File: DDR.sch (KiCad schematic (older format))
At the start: 41 parts, among them U1 IMX6UL_BGA289, U2 DDR3_BGA96

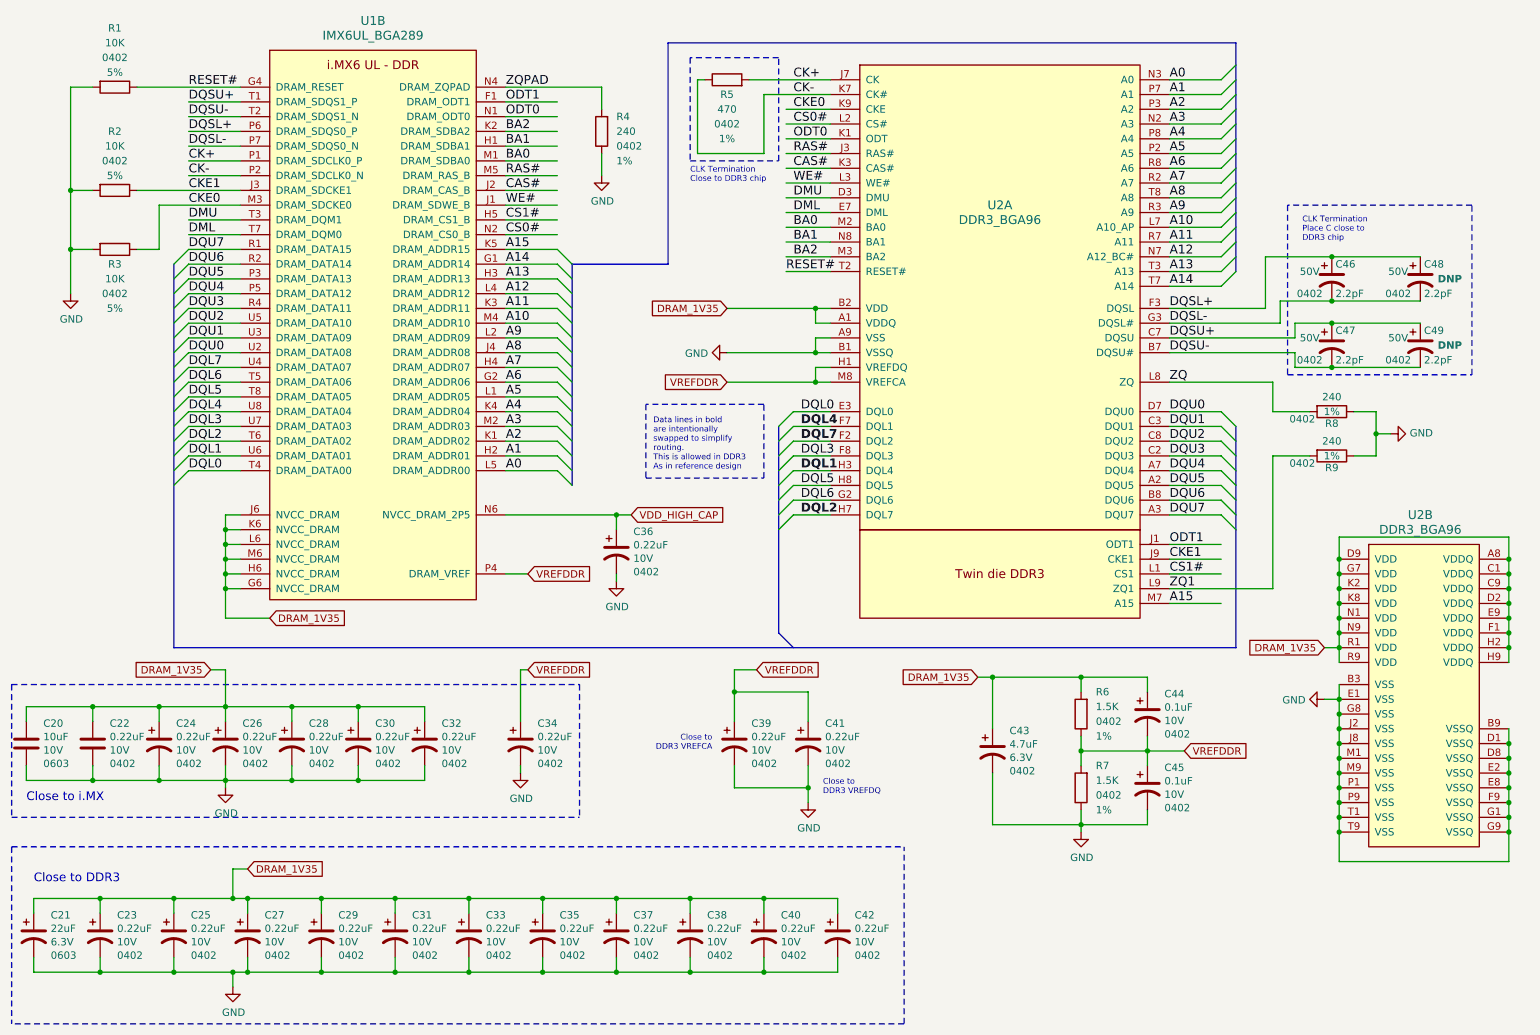
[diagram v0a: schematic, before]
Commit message: Added some LDO and connectors, still need to finish routing
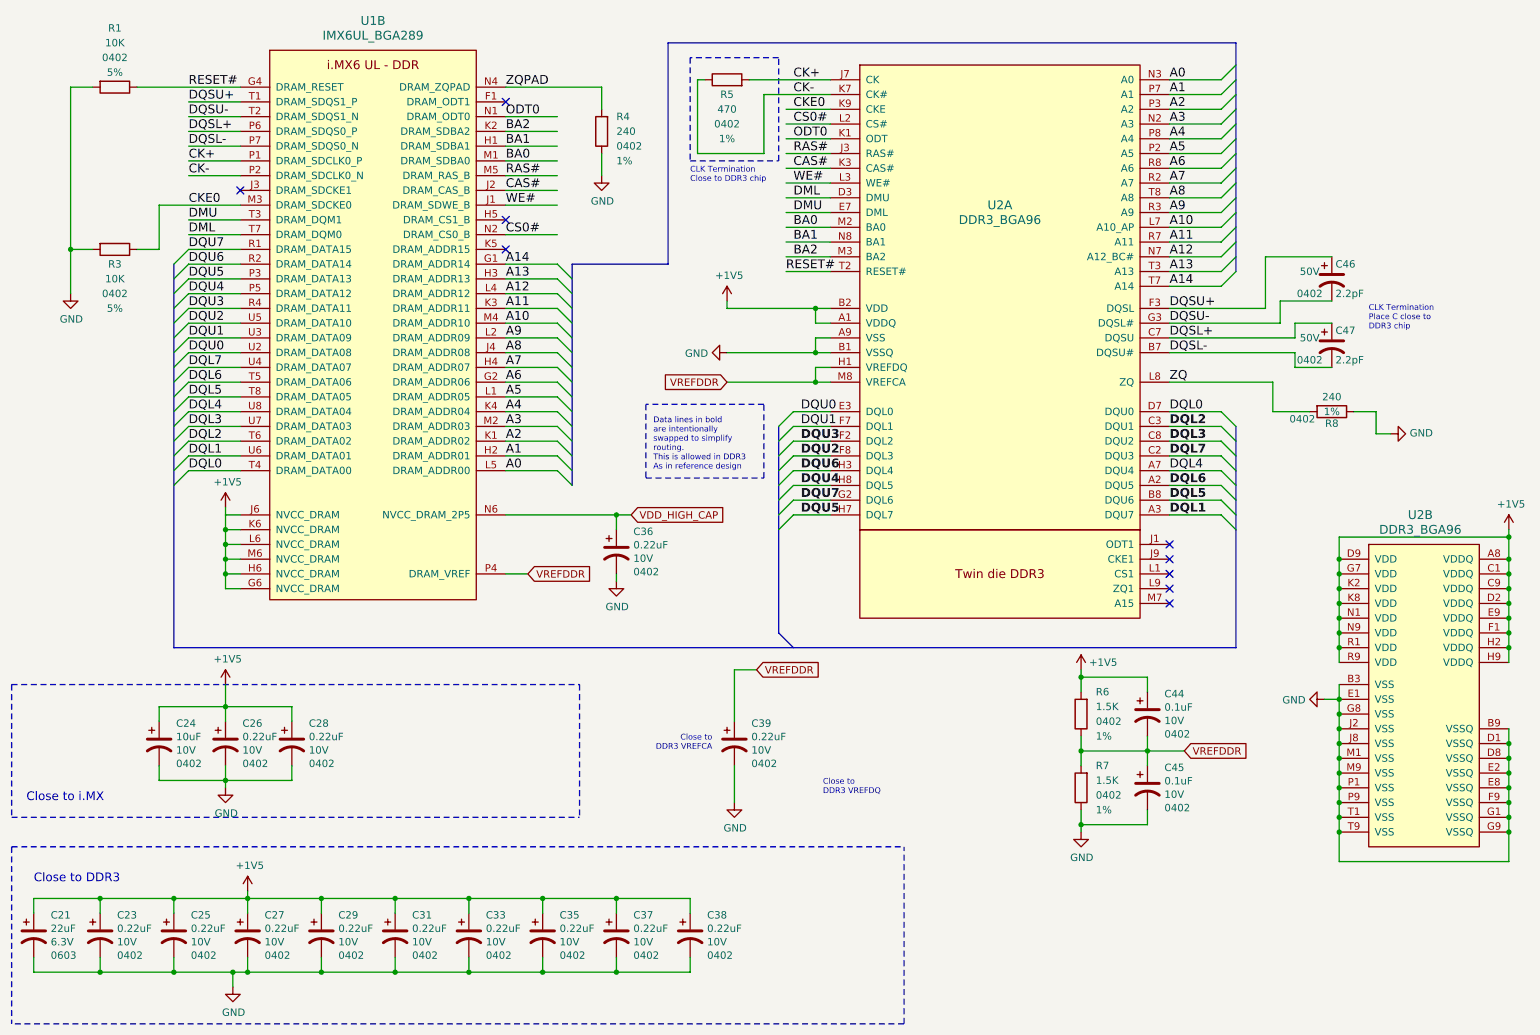
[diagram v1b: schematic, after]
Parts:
- removed C20: 10uF, Capacitor_SMD:C_0603_1608Metric, symbol Device:C
- removed C22: 0.22uF, Capacitor_SMD:C_0402_1005Metric, symbol Device:C
- removed C30, C32, C34, C40, C41, C42: 0.22uF, Capacitor_SMD:C_0402_1005Metric, symbol Device:CP1
- removed C43: 4.7uF, Capacitor_SMD:C_0402_1005Metric, symbol Device:CP1
- removed C48, C49: 2.2pF, Capacitor_SMD:C_0402_1005Metric, symbol nano-rescue:CP1
- removed R2: 10K, Resistor_SMD:R_0402_1005Metric, symbol Device:R
- removed R9: 240, Resistor_SMD:R_0402_1005Metric, symbol Device:R
- C24: value 0.22uF -> 10uF
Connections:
- net labels added: +1V5
- net labels removed: A15, CKE1, CS1#, DRAM_1V35, ODT1, ZQ1
- wire segments 323 -> 264
- no-connect marks 0 -> 9

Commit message: Finished first version of board
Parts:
- C21: LCSC (none) -> C59461; SMD (none) -> 0603; SMD size 0603 -> (none)
- C23, C25, C26, C27, C28, C29, C31, C33, C35, C36, C37, C38, C39: LCSC (none) -> C16772; SMD (none) -> 0402; SMD size 0402 -> (none)
- C24: footprint Capacitor_SMD:C_0402_1005Metric -> Capacitor_SMD:C_0603_1608Metric; LCSC (none) -> C15525; SMD (none) -> 0603; SMD size 0402 -> (none)
- C44, C45: LCSC (none) -> C1525; SMD (none) -> 0402; SMD size 0402 -> (none)
- C46, C47: LCSC (none) -> C1559; SMD (none) -> 0402; SMD Size 0402 -> (none)
- R1, R3: LCSC (none) -> C25744; SMD (none) -> 0402; SMD Size 0402 -> (none)
- R4, R8: LCSC (none) -> C25094; SMD (none) -> 0402; SMD Size 0402 -> (none)
- R5: LCSC (none) -> C25792; SMD (none) -> 0402; SMD Size 0402 -> (none)
- R6, R7: DNP DNP -> (none); LCSC (none) -> C25867; SMD (none) -> 0402; SMD Size 0402 -> (none)
- U1: LCSC (none) -> C414042
- U2: LCSC (none) -> C36513
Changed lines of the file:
@@
 F 2 "Custom Components:IMX6UL_BGA289" H 3100 -750 60  0001 C CNN
 F 3 "" H 3100 -750 60  0001 C CNN
+F 4 " C414042" H 3200 950 50  0001 C CNN "LCSC"
 	2    3200 950
 	1    0    0    -1
@@
 F 2 "Resistor_SMD:R_0402_1005Metric" V 9630 3400 50  0001 C CNN
 F 3 "" H 9700 3400 50  0000 C CNN
-F 4 "0402" V 9750 3200 50  0000 C CNN "SMD Size"
+F 4 "0402" V 9750 3200 50  0000 C CNN "SMD"
 F 5 "1%" V 9700 3400 50  0000 C CNN "Tolerance"
+F 6 "C25094" H 9700 3400 50  0001 C CNN "LCSC"
 	1    9700 3400
 	0    1    1    0
@@
 F 2 "Resistor_SMD:R_0402_1005Metric" V 4680 1500 50  0001 C CNN
 F 3 "" H 4750 1500 50  0000 C CNN
-F 4 "0402" H 4650 1600 50  0000 R CNN "SMD Size"
+F 4 "0402" H 4650 1600 50  0000 R CNN "SMD"
 F 5 "1%" H 4650 1700 50  0000 R CNN "Tolerance"
+F 6 "C25094" H 4750 1500 50  0001 C CNN "LCSC"
 	1    4750 1500
 	-1   0    0    1
@@
 F 2 "Resistor_SMD:R_0402_1005Metric" V 5530 1150 50  0001 C CNN
 F 3 "" H 5600 1150 50  0000 C CNN
-F 4 "0402" V 5300 1150 50  0000 C CNN "SMD Size"
+F 4 "0402" V 5300 1150 50  0000 C CNN "SMD"
 F 5 "1%" V 5200 1150 50  0000 C CNN "Tolerance"
+F 6 "C25792" H 5600 1150 50  0001 C CNN "LCSC"
 	1    5600 1150
 	0    -1   -1   0
@@
 F 2 "Capacitor_SMD:C_0402_1005Metric" H 9700 2500 50  0001 C CNN
 F 3 "" H 9700 2500 50  0000 C CNN
-F 4 "0402" H 9550 2400 50  0000 C CNN "SMD Size"
+F 4 "0402" H 9550 2400 50  0000 C CNN "SMD"
 F 5 "50V" H 9550 2550 50  0000 C CNN "Voltage"
+F 6 "C1559" H 9700 2500 50  0001 C CNN "LCSC"
 	1    9700 2500
 	1    0    0    -1
@@
 F 2 "Capacitor_SMD:C_0402_1005Metric" H 9700 2950 50  0001 C CNN
 F 3 "" H 9700 2950 50  0000 C CNN
-F 4 "0402" H 9550 2850 50  0000 C CNN "SMD Size"
+F 4 "0402" H 9550 2850 50  0000 C CNN "SMD"
 F 5 "50V" H 9550 3000 50  0000 C CNN "Voltage"
+F 6 "C1559" H 9700 2950 50  0001 C CNN "LCSC"
 	1    9700 2950
 	1    0    0    -1
@@
 F 2 "Resistor_SMD:R_0402_1005Metric" V 1380 2300 50  0001 C CNN
 F 3 "" H 1450 2300 50  0000 C CNN
-F 4 "0402" V 1750 2300 50  0000 C CNN "SMD Size"
+F 4 "0402" V 1750 2300 50  0000 C CNN "SMD"
 F 5 "5%" V 1850 2300 50  0000 C CNN "Tolerance"
+F 6 "C25744" H 1450 2300 50  0001 C CNN "LCSC"
 	1    1450 2300
 	0    1    1    0
@@
 F 2 "Resistor_SMD:R_0402_1005Metric" V 1380 1200 50  0001 C CNN
 F 3 "" H 1450 1200 50  0000 C CNN
-F 4 "0402" V 1250 1200 50  0000 C CNN "SMD Size"
+F 4 "0402" V 1250 1200 50  0000 C CNN "SMD"
 F 5 "5%" V 1350 1200 50  0000 C CNN "Tolerance"
+F 6 "C25744" H 1450 1200 50  0001 C CNN "LCSC"
 	1    1450 1200
 	0    1    1    0
@@
 F 1 "DDR3_BGA96" H 7450 2300 60  0000 C CNN
 F 2 "Custom Components:DDR3_BGA96" H 7450 2200 60  0001 C CNN
-F 3 "" H 7450 2200 60  0001 C CNN
+F 3 "https://datasheet.lcsc.com/szlcsc/2006121213_Alliance-Memory-AS4C128M16D3LB-12BIN_C570201.pdf" H 7450 2200 60  0001 C CNN
+F 4 "C36513" H 7450 2200 50  0001 C CNN "LCSC"
 	1    7450 2200
 	1    0    0    -1
@@
 F 1 "DDR3_BGA96" H 10300 4400 60  0000 C CNN
 F 2 "Custom Components:DDR3_BGA96" H 10300 4300 60  0001 C CNN
-F 3 "" H 10300 4300 60  0001 C CNN
+F 3 "https://datasheet.lcsc.com/szlcsc/2006121213_Alliance-Memory-AS4C128M16D3LB-12BIN_C570201.pdf" H 10300 4300 60  0001 C CNN
+F 4 "C36513" H 10300 4300 50  0001 C CNN "LCSC"
 	2    10300 4300
 	1    0    0    -1
@@
 F 3 "~" H 4850 4350 50  0001 C CNN
 F 4 "10V" H 4965 4305 50  0000 L CNN "Voltage"
-F 5 "0402" H 4965 4214 50  0000 L CNN "SMD size"
+F 5 "" H 4965 4214 50  0000 L CNN "SMD size"
+F 6 "0402" H 4850 4350 50  0001 C CNN "SMD"
+F 7 "C16772" H 4850 4350 50  0001 C CNN "LCSC"
 	1    4850 4350
 	1    0    0    -1
@@
 F 0 "C24" H 1865 5787 50  0000 L CNN
 F 1 "10uF" H 1865 5696 50  0000 L CNN
-F 2 "Capacitor_SMD:C_0402_1005Metric" H 1750 5650 50  0001 C CNN
+F 2 "Capacitor_SMD:C_0603_1608Metric" H 1750 5650 50  0001 C CNN
 F 3 "~" H 1750 5650 50  0001 C CNN
 F 4 "10V" H 1865 5605 50  0000 L CNN "Voltage"
-F 5 "0402" H 1865 5514 50  0000 L CNN "SMD size"
+F 5 "" H 1865 5514 50  0000 L CNN "SMD size"
+F 6 "0603" H 1750 5650 50  0001 C CNN "SMD"
+F 7 "C15525" H 1750 5650 50  0001 C CNN "LCSC"
 	1    1750 5650
 	1    0    0    -1
@@
 F 3 "~" H 2200 5650 50  0001 C CNN
 F 4 "10V" H 2315 5605 50  0000 L CNN "Voltage"
-F 5 "0402" H 2315 5514 50  0000 L CNN "SMD size"
+F 5 "" H 2315 5514 50  0000 L CNN "SMD size"
+F 6 "0402" H 2200 5650 50  0001 C CNN "SMD"
+F 7 "C16772" H 2200 5650 50  0001 C CNN "LCSC"
 	1    2200 5650
 	1    0    0    -1
@@
 F 3 "~" H 2650 5650 50  0001 C CNN
 F 4 "10V" H 2765 5605 50  0000 L CNN "Voltage"
-F 5 "0402" H 2765 5514 50  0000 L CNN "SMD size"
+F 5 "" H 2765 5514 50  0000 L CNN "SMD size"
+F 6 "0402" H 2650 5650 50  0001 C CNN "SMD"
+F 7 "C16772" H 2650 5650 50  0001 C CNN "LCSC"
 	1    2650 5650
 	1    0    0    -1
@@
 F 3 "~" H 900 6950 50  0001 C CNN
 F 4 "6.3V" H 1015 6905 50  0000 L CNN "Voltage"
-F 5 "0603" H 1015 6814 50  0000 L CNN "SMD size"
+F 5 "" H 1015 6814 50  0000 L CNN "SMD size"
+F 6 "0603" H 900 6950 50  0001 C CNN "SMD"
+F 7 "C59461" H 900 6950 50  0001 C CNN "LCSC"
 	1    900  6950
 	1    0    0    -1
@@
 F 3 "~" H 1350 6950 50  0001 C CNN
 F 4 "10V" H 1465 6905 50  0000 L CNN "Voltage"
-F 5 "0402" H 1465 6814 50  0000 L CNN "SMD size"
+F 5 "" H 1465 6814 50  0000 L CNN "SMD size"
+F 6 "0402" H 1350 6950 50  0001 C CNN "SMD"
+F 7 "C16772" H 1350 6950 50  0001 C CNN "LCSC"
 	1    1350 6950
 	1    0    0    -1
@@
 F 3 "~" H 1850 6950 50  0001 C CNN
 F 4 "10V" H 1965 6905 50  0000 L CNN "Voltage"
-F 5 "0402" H 1965 6814 50  0000 L CNN "SMD size"
+F 5 "" H 1965 6814 50  0000 L CNN "SMD size"
+F 6 "0402" H 1850 6950 50  0001 C CNN "SMD"
+F 7 "C16772" H 1850 6950 50  0001 C CNN "LCSC"
 	1    1850 6950
 	1    0    0    -1
@@
 F 3 "~" H 2350 6950 50  0001 C CNN
 F 4 "10V" H 2465 6905 50  0000 L CNN "Voltage"
-F 5 "0402" H 2465 6814 50  0000 L CNN "SMD size"
+F 5 "" H 2465 6814 50  0000 L CNN "SMD size"
+F 6 "0402" H 2350 6950 50  0001 C CNN "SMD"
+F 7 "C16772" H 2350 6950 50  0001 C CNN "LCSC"
 	1    2350 6950
 	1    0    0    -1
@@
 F 3 "~" H 2850 6950 50  0001 C CNN
 F 4 "10V" H 2965 6905 50  0000 L CNN "Voltage"
-F 5 "0402" H 2965 6814 50  0000 L CNN "SMD size"
+F 5 "" H 2965 6814 50  0000 L CNN "SMD size"
+F 6 "0402" H 2850 6950 50  0001 C CNN "SMD"
+F 7 "C16772" H 2850 6950 50  0001 C CNN "LCSC"
 	1    2850 6950
 	1    0    0    -1
@@
 F 3 "~" H 3350 6950 50  0001 C CNN
 F 4 "10V" H 3465 6905 50  0000 L CNN "Voltage"
-F 5 "0402" H 3465 6814 50  0000 L CNN "SMD size"
+F 5 "" H 3465 6814 50  0000 L CNN "SMD size"
+F 6 "0402" H 3350 6950 50  0001 C CNN "SMD"
+F 7 "C16772" H 3350 6950 50  0001 C CNN "LCSC"
 	1    3350 6950
 	1    0    0    -1
@@
 F 3 "~" H 3850 6950 50  0001 C CNN
 F 4 "10V" H 3965 6905 50  0000 L CNN "Voltage"
-F 5 "0402" H 3965 6814 50  0000 L CNN "SMD size"
+F 5 "" H 3965 6814 50  0000 L CNN "SMD size"
+F 6 "0402" H 3850 6950 50  0001 C CNN "SMD"
+F 7 "C16772" H 3850 6950 50  0001 C CNN "LCSC"
 	1    3850 6950
 	1    0    0    -1
@@
 F 3 "~" H 4350 6950 50  0001 C CNN
 F 4 "10V" H 4465 6905 50  0000 L CNN "Voltage"
-F 5 "0402" H 4465 6814 50  0000 L CNN "SMD size"
+F 5 "" H 4465 6814 50  0000 L CNN "SMD size"
+F 6 "0402" H 4350 6950 50  0001 C CNN "SMD"
+F 7 "C16772" H 4350 6950 50  0001 C CNN "LCSC"
 	1    4350 6950
 	1    0    0    -1
@@
 F 3 "~" H 4850 6950 50  0001 C CNN
 F 4 "10V" H 4965 6905 50  0000 L CNN "Voltage"
-F 5 "0402" H 4965 6814 50  0000 L CNN "SMD size"
+F 5 "" H 4965 6814 50  0000 L CNN "SMD size"
+F 6 "0402" H 4850 6950 50  0001 C CNN "SMD"
+F 7 "C16772" H 4850 6950 50  0001 C CNN "LCSC"
 	1    4850 6950
 	1    0    0    -1
@@
 F 3 "~" H 5350 6950 50  0001 C CNN
 F 4 "10V" H 5465 6905 50  0000 L CNN "Voltage"
-F 5 "0402" H 5465 6814 50  0000 L CNN "SMD size"
+F 5 "" H 5465 6814 50  0000 L CNN "SMD size"
+F 6 "0402" H 5350 6950 50  0001 C CNN "SMD"
+F 7 "C16772" H 5350 6950 50  0001 C CNN "LCSC"
 	1    5350 6950
 	1    0    0    -1
@@
 F 3 "~" H 5650 5650 50  0001 C CNN
 F 4 "10V" H 5765 5605 50  0000 L CNN "Voltage"
-F 5 "0402" H 5765 5514 50  0000 L CNN "SMD size"
+F 5 "" H 5765 5514 50  0000 L CNN "SMD size"
+F 6 "0402" H 5650 5650 50  0001 C CNN "SMD"
+F 7 "C16772" H 5650 5650 50  0001 C CNN "LCSC"
 	1    5650 5650
 	1    0    0    -1
@@
 F 3 "~" H 8450 5450 50  0001 C CNN
 F 4 "10V" H 8565 5405 50  0000 L CNN "Voltage"
-F 5 "0402" H 8565 5314 50  0000 L CNN "SMD size"
+F 5 "0402" H 8565 5314 50  0000 L CNN "SMD"
+F 6 "C1525" H 8450 5450 50  0001 C CNN "LCSC"
 	1    8450 5450
 	1    0    0    -1
@@
 F 2 "Resistor_SMD:R_0402_1005Metric" V 7930 5450 50  0001 C CNN
 F 3 "" H 8000 5450 50  0000 C CNN
-F 4 "0402" H 7900 5500 50  0000 R CNN "SMD Size"
+F 4 "0402" H 7900 5500 50  0000 R CNN "SMD"
 F 5 "1%" H 7900 5600 50  0000 R CNN "Tolerance"
-F 6 "DNP" H 8150 5450 50  0001 C CNB "DNP"
+F 6 "C25867" H 8000 5450 50  0001 C CNN "LCSC"
 	1    8000 5450
 	-1   0    0    1
@@
 F 3 "~" H 8450 5950 50  0001 C CNN
 F 4 "10V" H 8565 5905 50  0000 L CNN "Voltage"
-F 5 "0402" H 8565 5814 50  0000 L CNN "SMD size"
+F 5 "0402" H 8565 5814 50  0000 L CNN "SMD"
+F 6 "C1525" H 8450 5950 50  0001 C CNN "LCSC"
 	1    8450 5950
 	1    0    0    -1
@@
 F 2 "Resistor_SMD:R_0402_1005Metric" V 7930 5950 50  0001 C CNN
 F 3 "" H 8000 5950 50  0000 C CNN
-F 4 "0402" H 7900 6000 50  0000 R CNN "SMD Size"
+F 4 "0402" H 7900 6000 50  0000 R CNN "SMD"
 F 5 "1%" H 7900 6100 50  0000 R CNN "Tolerance"
-F 6 "DNP" H 8150 5950 50  0001 C CNB "DNP"
+F 6 "C25867" H 8000 5950 50  0001 C CNN "LCSC"
 	1    8000 5950
 	-1   0    0    1
